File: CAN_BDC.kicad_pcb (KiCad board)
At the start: 2 copper layers, 27 parts, among them P1 CONN_01X02, P2 CONN_01X05, P3 CONN_01X02, P4 CONN_01X02, P5 CONN_01X02, P6 CONN_01X02, P7 CONN_01X04, U1 PSD2CAN, U2 SN65HVD232D, U3 POLOLU_A4988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

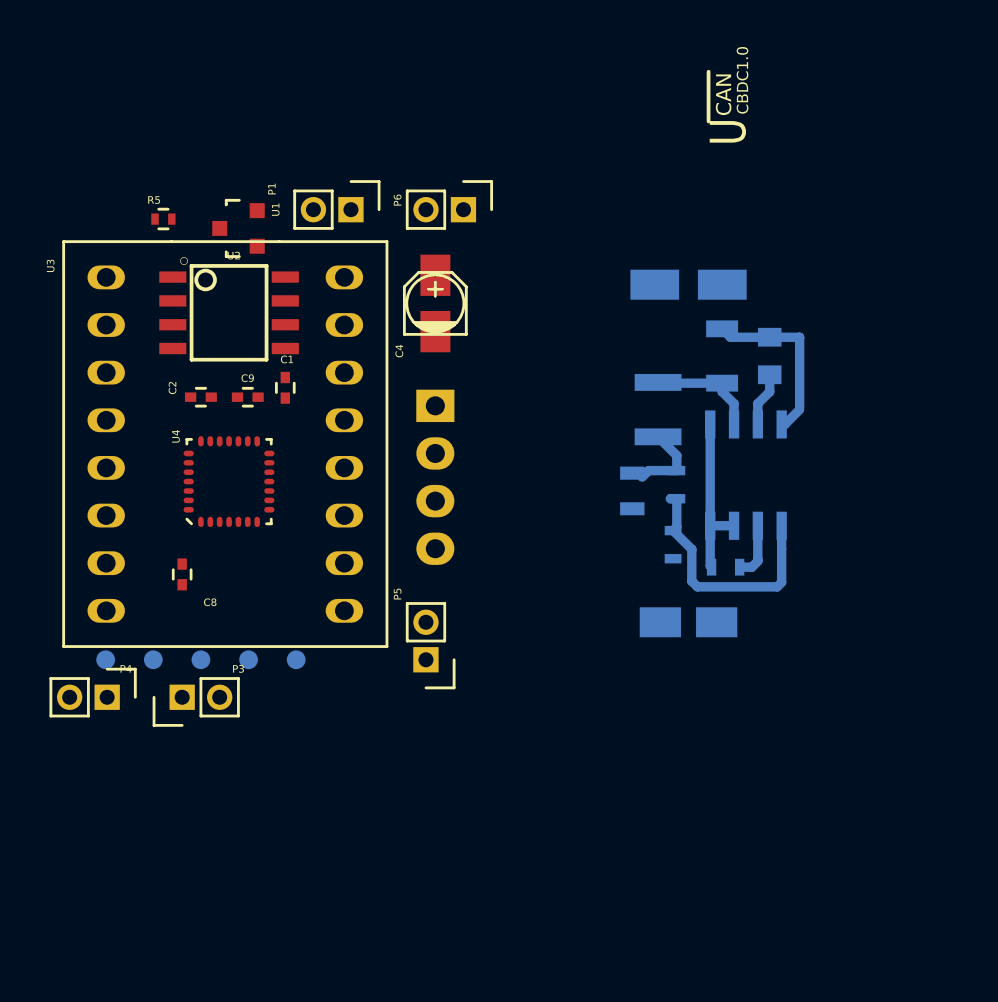
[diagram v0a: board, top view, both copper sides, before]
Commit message: step up converter routing
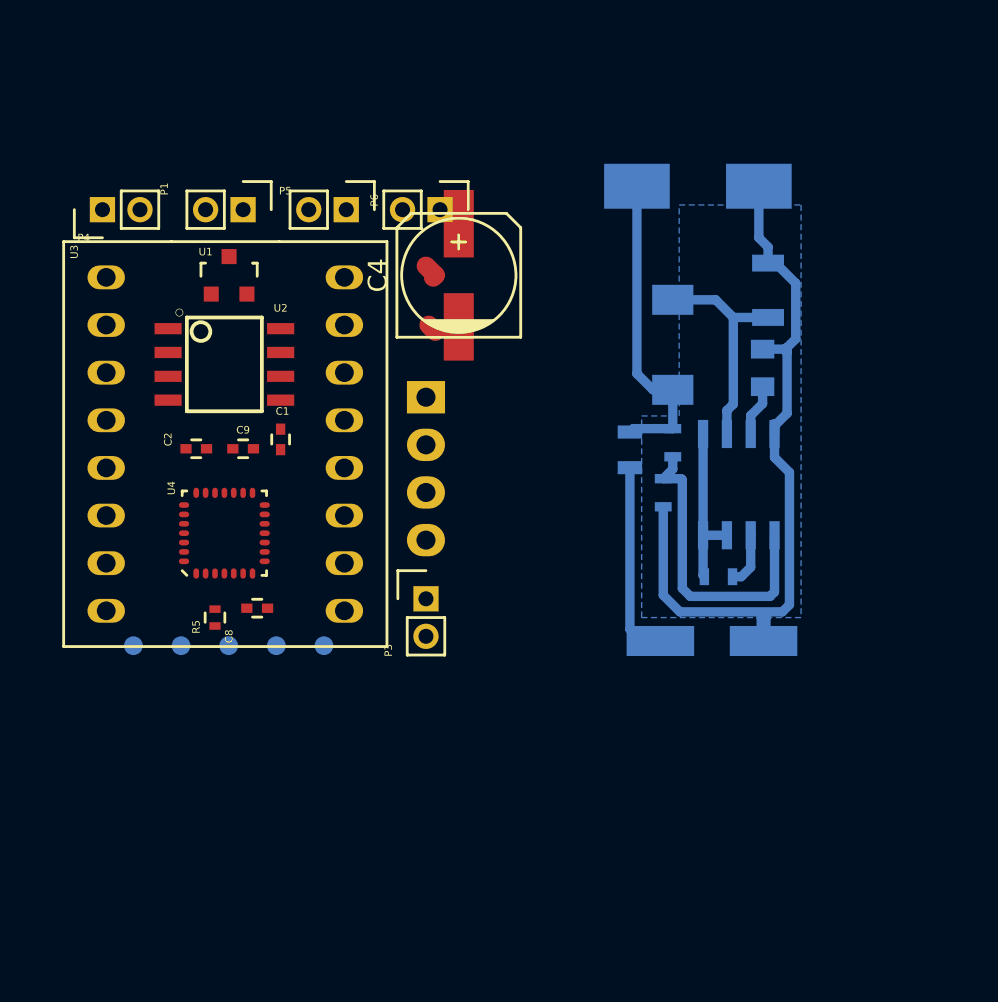
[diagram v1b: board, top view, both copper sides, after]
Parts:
- C4: footprint Capacitors_SMD:c_elec_3x5.3 -> Capacitors_SMD:c_elec_6.3x7.7
- C6: footprint Capacitors_SMD:c_elec_4x5.8 -> Capacitors_SMD:c_elec_8x10
- C7: value 100n -> 100u; footprint Capacitors_SMD:c_elec_3x5.3 -> Capacitors_SMD:c_elec_6.3x5.8
- L1: footprint Resistors_SMD:R_1210 -> usb_ccb_custom:DE0704_Coil
- moved P4 26.0 mm to (140.7, 86.3), turned to 90 degrees
- moved P5 24.4 mm to (153.7, 86.3), turned to 270 degrees
- moved R5 21.4 mm to (146.7, 108.0), turned to 270 degrees
- moved P3 14.0 mm to (157.9, 107.0), turned to 0 degrees
- moved L1 5.91 mm to (171.1, 91.1), turned to 0 degrees
- moved P1 5.75 mm to (148.2, 86.3)
- moved C6 5.27 mm to (172.4, 85.0)
- moved C8 4.39 mm to (148.9, 107.5), turned to 0 degrees
- moved D1 4.28 mm to (176.1, 90.6)
- moved R1 2.82 mm to (170.6, 101.4)
- moved C1 2.76 mm to (150.2, 98.5)
- moved C2 2.76 mm to (145.7, 99.0)
- moved C9 2.76 mm to (148.2, 99.0)
- moved U2 2.76 mm to (147.2, 94.5)
- moved U4 2.76 mm to (147.2, 103.5)
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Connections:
- C4 pad 2: GNDA -> GND
- C5 pad 2: GNDA -> GND
- C6 pad 2: GNDA -> GND
- D1 pad 2: GNDA -> GND
- P5 pad 1: Net-(P5-Pad1) -> (no net)
- P5 pad 2: Net-(P5-Pad2) -> (no net)
- P6 pad 1: GNDA -> GND
- R1 pad 2: GNDA -> GND
- U2 pad 5: Net-(U2-Pad5) -> (no net)
- U3 pad 15: GNDA -> GND
- U3 pad 9: GNDA -> GND
- U4 pad 11: Net-(U4-Pad11) -> (no net)
- U4 pad 12: Net-(U4-Pad12) -> (no net)
- U4 pad 13: Net-(U4-Pad13) -> (no net)
- U4 pad 14: Net-(U4-Pad14) -> (no net)
- U4 pad 19: Net-(U4-Pad19) -> (no net)
- U4 pad 6: Net-(U4-Pad6) -> (no net)
- U4 pad 7: Net-(U4-Pad7) -> (no net)
- U4 pad 8: Net-(U4-Pad8) -> (no net)
- U5 pad 4: GNDA -> GND
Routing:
- net GND: track 0.00 -> 39.7 mm
- net Net-(C6-Pad1): track 4.21 -> 16.7 mm
- net GNDA: track 9.31 -> 0.00 mm
- net +3V3: track 0.00 -> 9.15 mm
- net Net-(D1-Pad1): track 5.89 -> 12.0 mm
- net Net-(R1-Pad1): track 13.3 -> 16.4 mm
- net (no net): track 0.00 -> 1.36 mm
- added copper zone on B.Cu, net GND

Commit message: Footprints update
Footprints update
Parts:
- added R4: 120, Resistors_SMD:R_0402, F.Cu at (147.5, 88.3)
- C2: value 10u -> 10n
- C4: value 100uF -> 100u
- C6: value 470u -> 330u; footprint Capacitors_SMD:c_elec_8x10 -> Capacitors_SMD:c_elec_6.3x7.7
- C7: footprint Capacitors_SMD:c_elec_6.3x5.8 -> Capacitors_SMD:c_elec_5x5.8
- P2, P7: moved to F.Cu
- moved P5 29.1 mm to (141.6, 112.8)
- moved C1 8.01 mm to (143.0, 95.0), turned to 90 degrees
- moved P6 7.19 mm to (151.5, 86.2), turned to 90 degrees
- moved C7 4.03 mm to (170.3, 106.5), turned to 90 degrees
- moved P1 2.35 mm to (145.8, 86.2), turned to 90 degrees
- moved U2 1.32 mm to (147.8, 95.7)
- moved C6 0.98 mm to (172.8, 86.0), turned to 0 degrees
- moved R2 0.96 mm to (174.4, 105.5)
- moved U1 0.96 mm to (147.5, 90.8), turned to 180 degrees
- moved C4 0.95 mm to (159.6, 88.8)
- moved P7 0.73 mm to (157.8, 95.6), turned to 0 degrees
- moved P2 0.64 mm to (148.5, 110.2)
- moved R5 0.49 mm to (146.4, 107.6), turned to 0 degrees
- moved P4 0.45 mm to (140.2, 86.2)
- moved P3 0.32 mm to (157.6, 107.0)
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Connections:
- P5 pad 1: (no net) -> Net-(P5-Pad1)
- P5 pad 2: (no net) -> Net-(P5-Pad2)
- U2 pad 5: (no net) -> Net-(U2-Pad5)
- U4 pad 11: (no net) -> Net-(U4-Pad11)
- U4 pad 12: (no net) -> Net-(U4-Pad12)
- U4 pad 13: (no net) -> Net-(U4-Pad13)
- U4 pad 14: (no net) -> Net-(U4-Pad14)
- U4 pad 19: (no net) -> Net-(U4-Pad19)
- U4 pad 6: (no net) -> Net-(U4-Pad6)
- U4 pad 7: (no net) -> Net-(U4-Pad7)
- U4 pad 8: (no net) -> Net-(U4-Pad8)
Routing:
- net VPP: track 2.94 -> 31.2 mm
- net GND: track 39.7 -> 56.5 mm
- net +3V3: track 9.15 -> 15.5 mm
- net Net-(P7-Pad2): track 0.00 -> 4.51 mm
- net Net-(P7-Pad1): track 0.00 -> 4.51 mm
- net Net-(P7-Pad4): track 0.00 -> 4.51 mm
- net Net-(P7-Pad3): track 0.00 -> 4.51 mm
- net Net-(R2-Pad1): track 11.1 -> 8.68 mm
- net (no net): track 1.36 -> 0.00 mm
- net Net-(R1-Pad1): track 16.4 -> 15.3 mm
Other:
- board outline added: 25 x 32.5 mm

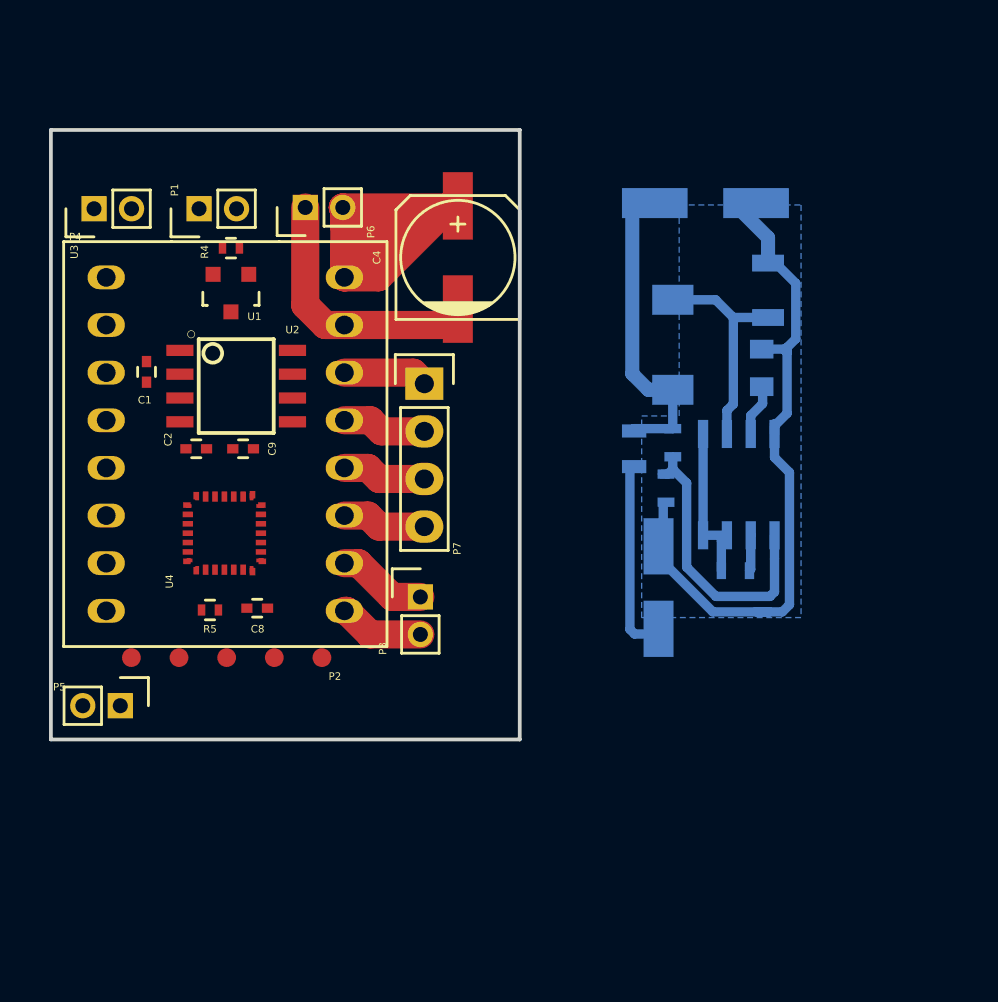
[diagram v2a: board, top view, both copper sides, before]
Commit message: Buck Converter Layout update.
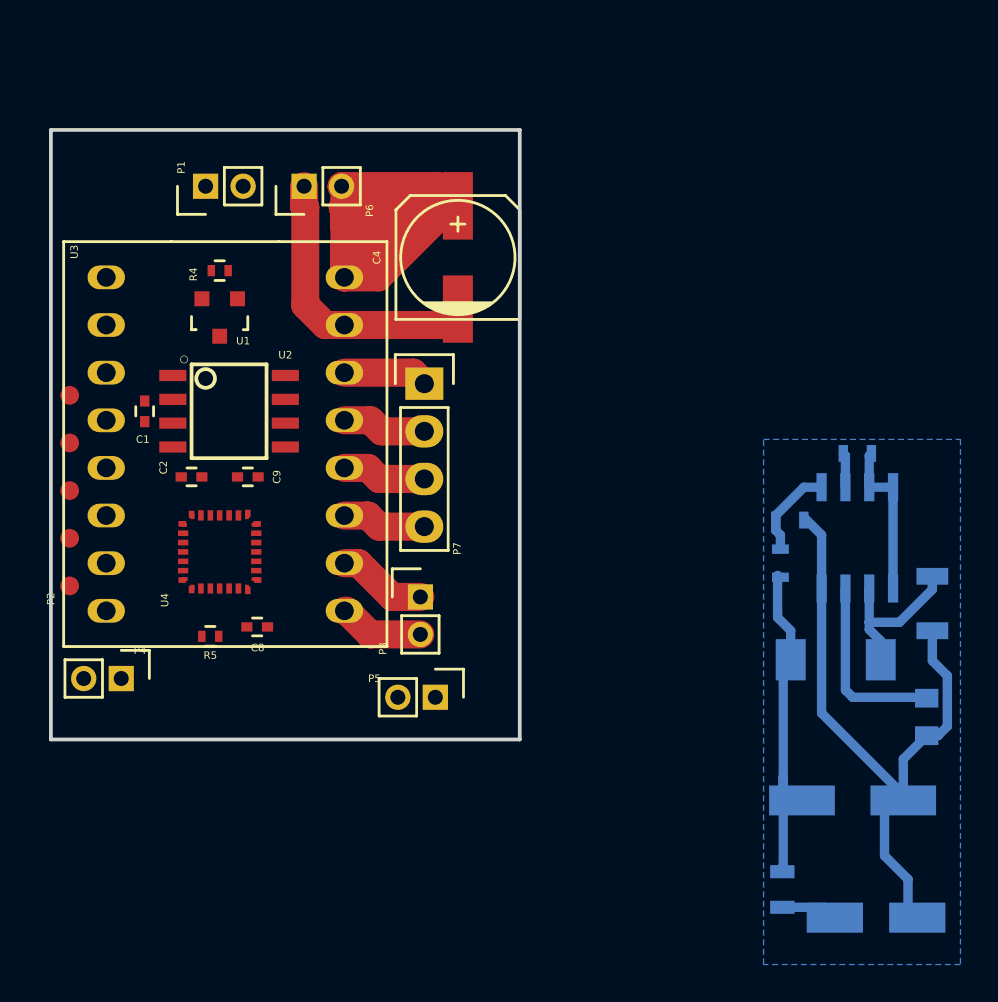
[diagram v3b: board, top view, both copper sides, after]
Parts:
- moved C6 32.8 mm to (180.7, 117.8)
- moved P4 25.1 mm to (141.7, 111.3), turned to 270 degrees
- moved L2 24.8 mm to (176.9, 122.5)
- moved L1 22.2 mm to (182.2, 110.3), turned to 270 degrees
- moved C7 21.1 mm to (181.9, 124.0), turned to 0 degrees
- moved C5 20.6 mm to (184.6, 113.3), turned to 270 degrees
- moved D1 18.9 mm to (184.9, 107.3), turned to 270 degrees
- moved P5 16.8 mm to (158.4, 112.3)
- moved P2 12.3 mm to (138.9, 102.5), turned to 90 degrees
- moved R2 9.02 mm to (180.9, 99.3), turned to 180 degrees
- moved R3 8.61 mm to (176.8, 105.2), turned to 270 degrees
- moved U5 6.93 mm to (180.9, 103.8), turned to 180 degrees
- moved R1 6.82 mm to (177.3, 102.8), turned to 0 degrees
- moved C1 2.10 mm to (142.9, 97.0)
- moved C2 1.52 mm to (145.4, 100.5)
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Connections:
- P5 pad 1: Net-(P5-Pad1) -> (no net)
- P5 pad 2: Net-(P5-Pad2) -> (no net)
- U2 pad 5: Net-(U2-Pad5) -> (no net)
- U4 pad 1: CAN_RX -> Net-(U4-Pad1)
- U4 pad 10: DRV_nENABLE -> (no net)
- U4 pad 11: Net-(U4-Pad11) -> (no net)
- U4 pad 12: Net-(U4-Pad12) -> (no net)
- U4 pad 13: Net-(U4-Pad13) -> DRV_MS1
- U4 pad 14: Net-(U4-Pad14) -> DRV_nENABLE
- U4 pad 19: Net-(U4-Pad19) -> CAN_RX
- U4 pad 6: Net-(U4-Pad6) -> (no net)
- U4 pad 9: DRV_MS1 -> (no net)
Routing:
- net Net-(R1-Pad1): track 15.3 -> 4.97 mm
- net VPP: track 31.2 -> 39.0 mm
- net Net-(C5-Pad1): track 2.91 -> 10.2 mm
- net +3V3: track 15.5 -> 8.50 mm
- net Net-(D1-Pad1): track 12.0 -> 8.84 mm
- net GND: track 56.5 -> 54.8 mm
- net Net-(C6-Pad1): track 17.1 -> 17.6 mm

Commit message: Layout improve
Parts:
- C4: moved to B.Cu
- moved P4 20.0 mm to (161.4, 108.3), turned to 180 degrees
- moved R3 14.8 mm to (175.8, 90.3)
- moved C5 14.8 mm to (183.6, 98.5)
- moved C6 14.8 mm to (179.7, 103.0)
- moved C7 14.8 mm to (180.9, 109.2)
- moved D1 14.8 mm to (183.9, 92.5)
- moved L1 14.8 mm to (181.2, 95.5)
- moved L2 14.8 mm to (175.9, 107.8)
- moved R1 14.8 mm to (176.3, 88.0)
- moved R2 14.8 mm to (179.9, 84.5)
- moved U5 14.8 mm to (179.9, 89.0)
- moved P5 11.9 mm to (161.4, 100.8), turned to 0 degrees
- moved C1 8.92 mm to (151.4, 94.3)
- moved P1 4.75 mm to (141.4, 85.0), turned to 270 degrees
- moved U1 2.47 mm to (148.2, 90.0)
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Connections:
- P2 pad 3: SW_CLK -> GND
- P2 pad 4: SW_DIO -> SW_CLK
- P2 pad 5: GND -> SW_DIO
- U4 pad 13: DRV_MS1 -> (no net)
- U4 pad 14: DRV_nENABLE -> Net-(U4-Pad14)
- U4 pad 23: DRV_MS2 -> DRV_nENABLE
- U4 pad 24: DRV_MS3 -> DRV_MS1
- U4 pad 25: DRV_nRESET -> DRV_MS2
- U4 pad 26: DRV_nSLEEP -> DRV_MS3
- U4 pad 27: /USART_RX -> DRV_nRESET
- U4 pad 28: /USART_TX -> DRV_nSLEEP
- U4 pad 8: Net-(U4-Pad8) -> /USART_TX
- U4 pad 9: (no net) -> /USART_RX
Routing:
- net GND: track 54.8 -> 23.6 mm, vias 0 -> 3
- net SW_CLK: track 0.00 -> 29.1 mm
- net SW_DIO: track 0.00 -> 27.2 mm
- net +3V3: track 8.50 -> 27.3 mm
- net DRV_nENABLE: track 0.00 -> 16.5 mm
- net DRV_MS1: track 0.00 -> 14.6 mm
- net Net-(P2-Pad2): track 0.00 -> 14.5 mm
- net DRV_MS2: track 0.00 -> 12.6 mm
- net DRV_MS3: track 0.00 -> 10.7 mm
- net VPP: track 39.0 -> 49.6 mm, vias 0 -> 3
- net DRV_nRESET: track 0.00 -> 8.71 mm
- net DRV_STEP: track 0.00 -> 7.26 mm
- net DRV_DIR: track 0.00 -> 7.16 mm
- net DRV_nSLEEP: track 0.00 -> 7.08 mm
- net Net-(P1-Pad2): track 0.00 -> 5.54 mm
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- added copper zone on F.Cu, net GND
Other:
- board size 25 x 32.5 mm -> 26 x 28 mm

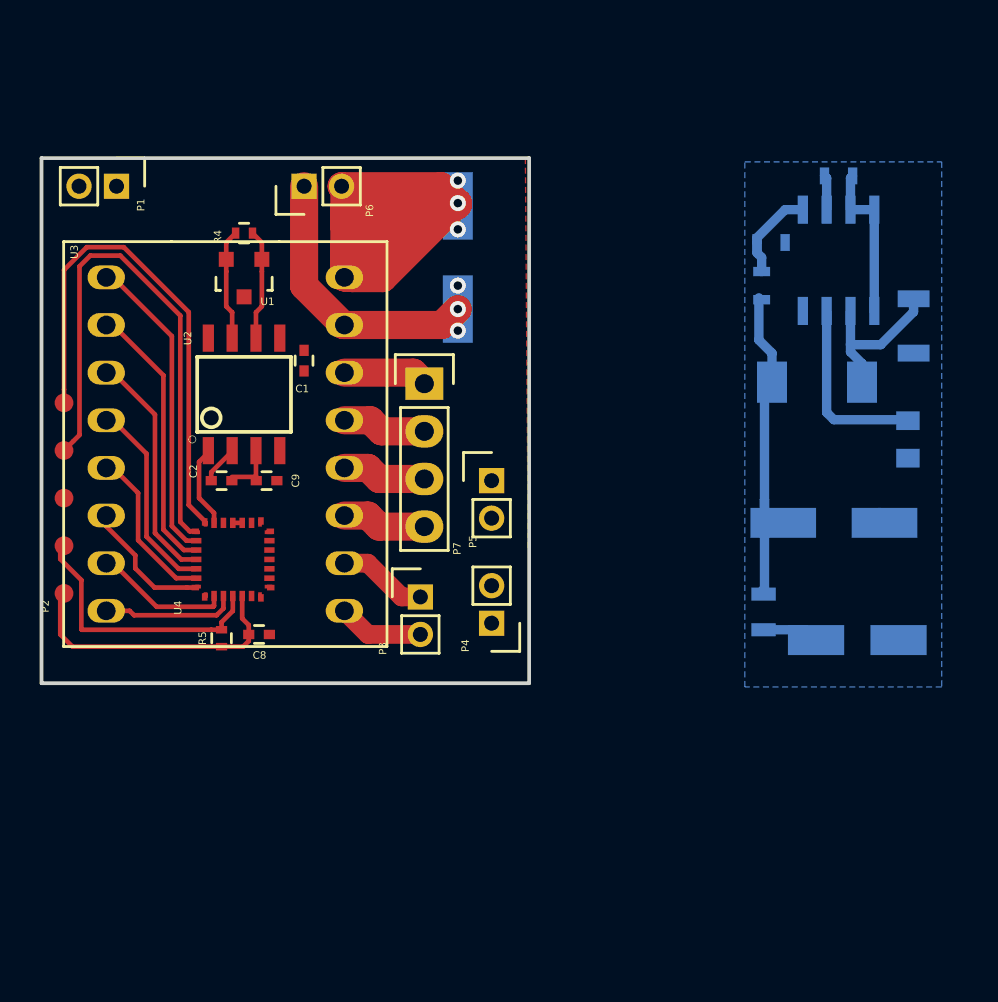
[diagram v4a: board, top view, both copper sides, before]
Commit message: Bootconnector addition
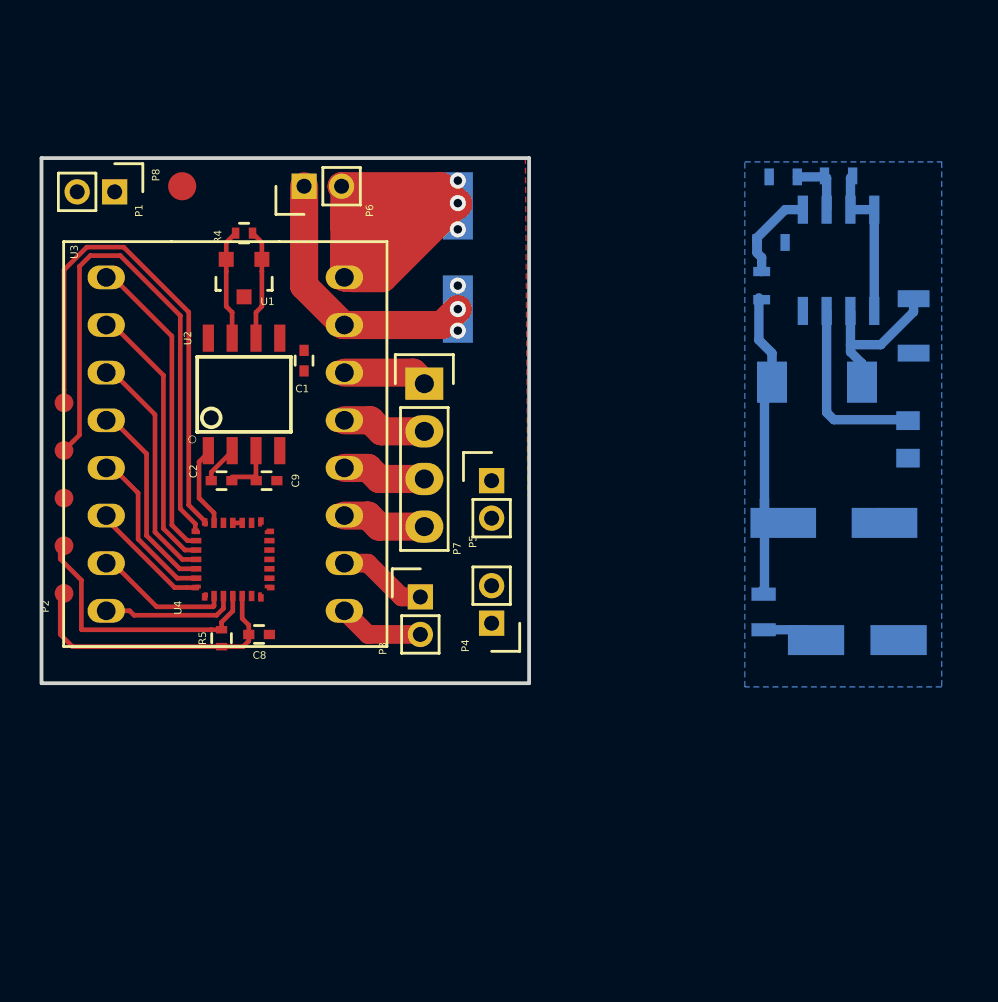
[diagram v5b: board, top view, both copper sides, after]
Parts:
- added P8: CONN_01X01, usb_ccb_custom:smd1Conn, F.Cu at (144.9, 85.0)
- added R6: 0, Resistors_SMD:R_0603, B.Cu at (176.9, 84.5)
- moved P1 0.32 mm to (141.3, 85.3)
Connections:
- P5 pad 1: (no net) -> Net-(P5-Pad1)
- P5 pad 2: (no net) -> Net-(P5-Pad2)
- R2 pad 2: VPP -> Net-(R2-Pad2)
- U2 pad 5: (no net) -> Net-(U2-Pad5)
- U4 pad 10: (no net) -> Net-(U4-Pad10)
- U4 pad 11: (no net) -> Net-(U4-Pad11)
- U4 pad 12: (no net) -> Net-(U4-Pad12)
- U4 pad 13: (no net) -> Net-(U4-Pad13)
- U4 pad 151: CAN_MOD -> (no net)
- U4 pad 6: (no net) -> Net-(U4-Pad6)
- U4 pad 8q: /USART_TX -> (no net)
- U5 pad 6: VPP -> Net-(R2-Pad2)
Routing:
- net Net-(R2-Pad2): track 0.00 -> 3.32 mm
- net VPP: track 49.6 -> 47.8 mm
- net DRV_nSLEEP: track 7.08 -> 6.45 mm

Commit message: Fids addition
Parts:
- added P9: CONN_01X02, Pin_Headers:Pin_Header_Straight_1x02_Pitch2.00mm, F.Cu at (161.7, 96.3)
- added f1: fiducial, Fiducials:Fiducial_1mm_Dia_2.54mm_Outer_CopperTop, F.Cu at (161.4, 110.0)
- added f2: fiducial, Fiducials:Fiducial_1mm_Dia_2.54mm_Outer_CopperTop, F.Cu at (138.9, 85.5)
- added f3: fiducial, Fiducials:Fiducial_1mm_Dia_2.54mm_Outer_CopperBottom, F.Cu at (161.4, 110.0)
- added f4: fiducial, Fiducials:Fiducial_1mm_Dia_2.54mm_Outer_CopperBottom, F.Cu at (138.9, 85.5)
- moved C5 32.8 mm to (150.8, 98.5)
- moved C6 32.8 mm to (146.9, 103.0)
- moved C7 32.8 mm to (148.2, 109.2)
- moved D1 32.8 mm to (151.2, 92.5)
- moved L1 32.8 mm to (148.4, 95.5)
- moved L2 32.8 mm to (143.2, 107.8)
- moved R1 32.8 mm to (143.6, 88.0)
- moved R3 32.8 mm to (143.1, 90.3)
- moved U5 32.8 mm to (147.2, 89.0)
- moved R2 31.3 mm to (148.7, 84.5)
- moved R6 30.8 mm to (146.2, 84.5)
- moved P8 26.3 mm to (138.7, 110.5)
- moved P4 1.57 mm to (161.7, 106.8)
- moved P5 0.84 mm to (161.7, 101.5), turned to 180 degrees
- moved P1 0.73 mm to (142.0, 85.5), turned to 90 degrees
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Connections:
- P5 pad 1: Net-(P5-Pad1) -> /GPIO1
- P5 pad 2: Net-(P5-Pad2) -> /GPIO2
- U4 pad 10: Net-(U4-Pad10) -> /GPIO1
- U4 pad 11: Net-(U4-Pad11) -> /GPIO2
- U4 pad 12: Net-(U4-Pad12) -> /GPIO3
- U4 pad 13: Net-(U4-Pad13) -> /GPIO4
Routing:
- net Net-(P8-Pad1): track 0.00 -> 17.2 mm
- net CAN_RX: track 0.31 -> 7.18 mm
- net Net-(P1-Pad1): track 5.54 -> 12.4 mm
- net Net-(P1-Pad2): track 5.54 -> 11.1 mm
- net +3V3: track 27.3 -> 30.7 mm
- net CAN_MOD: track 0.00 -> 0.57 mm
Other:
- board size 26 x 28 mm -> 26 x 28.5 mm
